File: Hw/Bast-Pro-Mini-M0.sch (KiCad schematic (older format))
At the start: 18 parts, among them J1 USB_B_Micro, J2 Conn_02x02_Odd_Even, P1 Digital, P2 ADC, P3 Analog, SW1 SW_DPST_x2, U1 AP2112K-3.3TRG1, U2 ATSAMD21E18A-AF

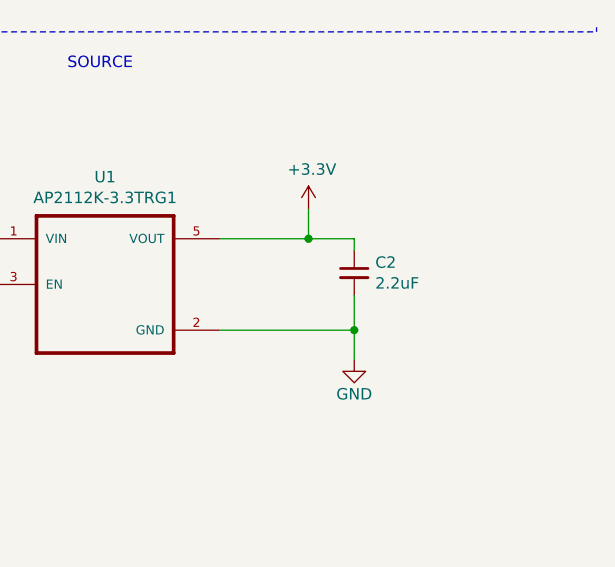
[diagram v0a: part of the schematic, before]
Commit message: Change caps
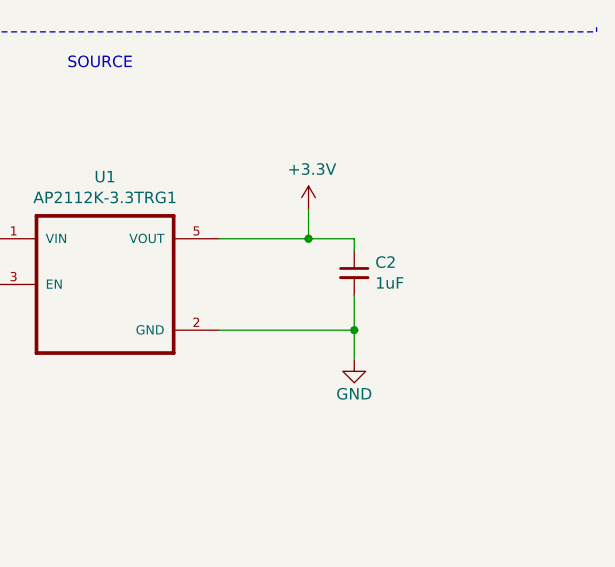
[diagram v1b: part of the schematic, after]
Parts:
- C2: value 2.2uF -> 1uF; manf# 885012106011 -> 885012106022
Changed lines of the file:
@@
 EESchema Schematic File Version 4
 LIBS:Bast-Pro-Mini-M0-cache
-EELAYER 26 0
+EELAYER 29 0
 EELAYER END
 $Descr A4 11693 8268
@@
 	2260 4200 2260 4070
 $Comp
-L Device:C_Small C1
-U 1 1 5BB50FD7
-P 8010 4850
-F 0 "C1" H 8102 4896 50  0000 L CNN
-F 1 "1uF" H 8102 4805 50  0000 L CNN
-F 2 "Capacitor_SMD:C_0603_1608Metric_Pad1.05x0.95mm_HandSolder" H 8010 4850 50  0001 C CNN
-F 3 "~" H 8010 4850 50  0001 C CNN
-F 4 "885012106022" H 8010 4850 50  0001 C CNN "manf#"
-	1    8010 4850
-	1    0    0    -1
-$EndComp
-$Comp
 L Bast-Pro-Mini-M0-rescue:AP2112K-3.3TRG1-Croketa-cache U1
 U 1 1 5BB540C8
@@
 F 3 "" H 9950 4390 50  0001 C CNN
 	1    9950 4390
-	1    0    0    -1
-$EndComp
-$Comp
-L Device:C_Small C2
-U 1 1 5BB62453
-P 10150 4670
-F 0 "C2" H 10242 4716 50  0000 L CNN
-F 1 "2.2uF" H 10242 4625 50  0000 L CNN
-F 2 "Capacitor_SMD:C_0603_1608Metric_Pad1.05x0.95mm_HandSolder" H 10150 4670 50  0001 C CNN
-F 3 "~" H 10150 4670 50  0001 C CNN
-F 4 "885012106011" H 10150 4670 50  0001 C CNN "manf#"
-	1    10150 4670
 	1    0    0    -1
 $EndComp
@@
 	2530 1220 2530 1170
 NoConn ~ 4430 1910
+$Comp
+L Device:C_Small C2
+U 1 1 5BB62453
+P 10150 4670
+F 0 "C2" H 10242 4716 50  0000 L CNN
+F 1 "1uF" H 10242 4625 50  0000 L CNN
+F 2 "Capacitor_SMD:C_0603_1608Metric_Pad1.05x0.95mm_HandSolder" H 10150 4670 50  0001 C CNN
+F 3 "~" H 10150 4670 50  0001 C CNN
+F 4 "885012106022" H 10150 4670 50  0001 C CNN "manf#"
+	1    10150 4670
+	1    0    0    -1
+$EndComp
+$Comp
+L Device:C_Small C1
+U 1 1 5BB50FD7
+P 8010 4850
+F 0 "C1" H 8102 4896 50  0000 L CNN
+F 1 "1uF" H 8102 4805 50  0000 L CNN
+F 2 "Capacitor_SMD:C_0603_1608Metric_Pad1.05x0.95mm_HandSolder" H 8010 4850 50  0001 C CNN
+F 3 "~" H 8010 4850 50  0001 C CNN
+F 4 "885012106022" H 8010 4850 50  0001 C CNN "manf#"
+	1    8010 4850
+	1    0    0    -1
+$EndComp
 $EndSCHEMATC

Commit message: Update USB v1.0
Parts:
- J1: footprint Connector_USB:USB_Micro-B_Wuerth_629105150521 -> Connectors:U254051N4BH806; manf# 629105150521 -> U254051N4BH806
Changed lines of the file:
@@
 Sheet 1 1
 Title "Bast Pro Mini M0"
-Date "2019-01-10"
-Rev "0.2"
+Date "2019-11-15"
+Rev "1"
 Comp "Electronic Cats"
 Comment1 "Edgar Capuchino"
@@
 F 0 "J1" H 1305 4867 50  0000 C CNN
 F 1 "USB_B_Micro" H 1305 4776 50  0000 C CNN
-F 2 "Connector_USB:USB_Micro-B_Wuerth_629105150521" H 1400 4350 50  0001 C CNN
+F 2 "Connectors:U254051N4BH806" H 1400 4350 50  0001 C CNN
 F 3 "~" H 1400 4350 50  0001 C CNN
-F 4 "629105150521" H 1250 4400 50  0001 C CNN "manf#"
+F 4 "U254051N4BH806" H 1250 4400 50  0001 C CNN "manf#"
 	1    1250 4400
 	1    0    0    -1
